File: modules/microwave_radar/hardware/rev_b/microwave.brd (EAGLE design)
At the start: 68.1 x 66 mm, 56 parts, among them J1 MODULE_GENERIC, J2 TC2030-JLINK-L, U1 SAM4LC8AA, U2 TLV62130, U3 MSGEQ7, U4 HB100, U5 OP284E_SEPARATE

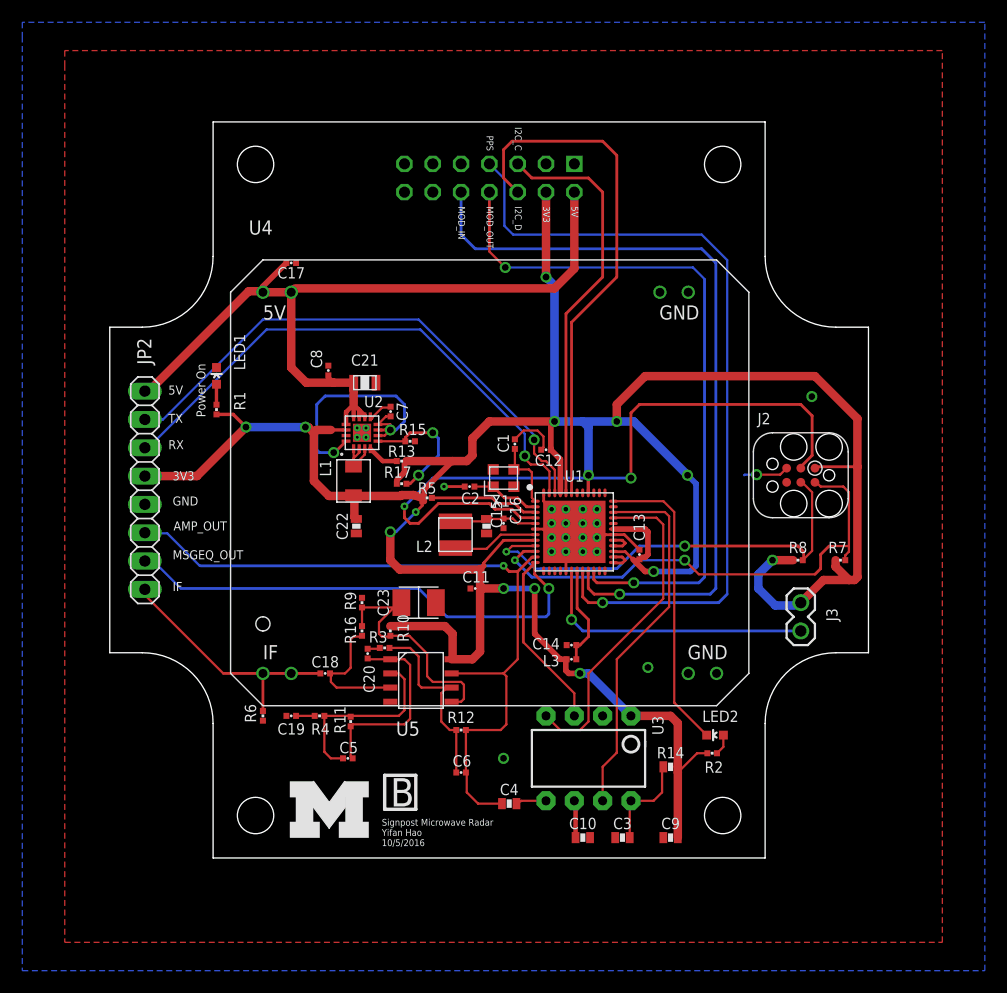
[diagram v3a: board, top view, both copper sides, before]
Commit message: added power gates, almost done routing
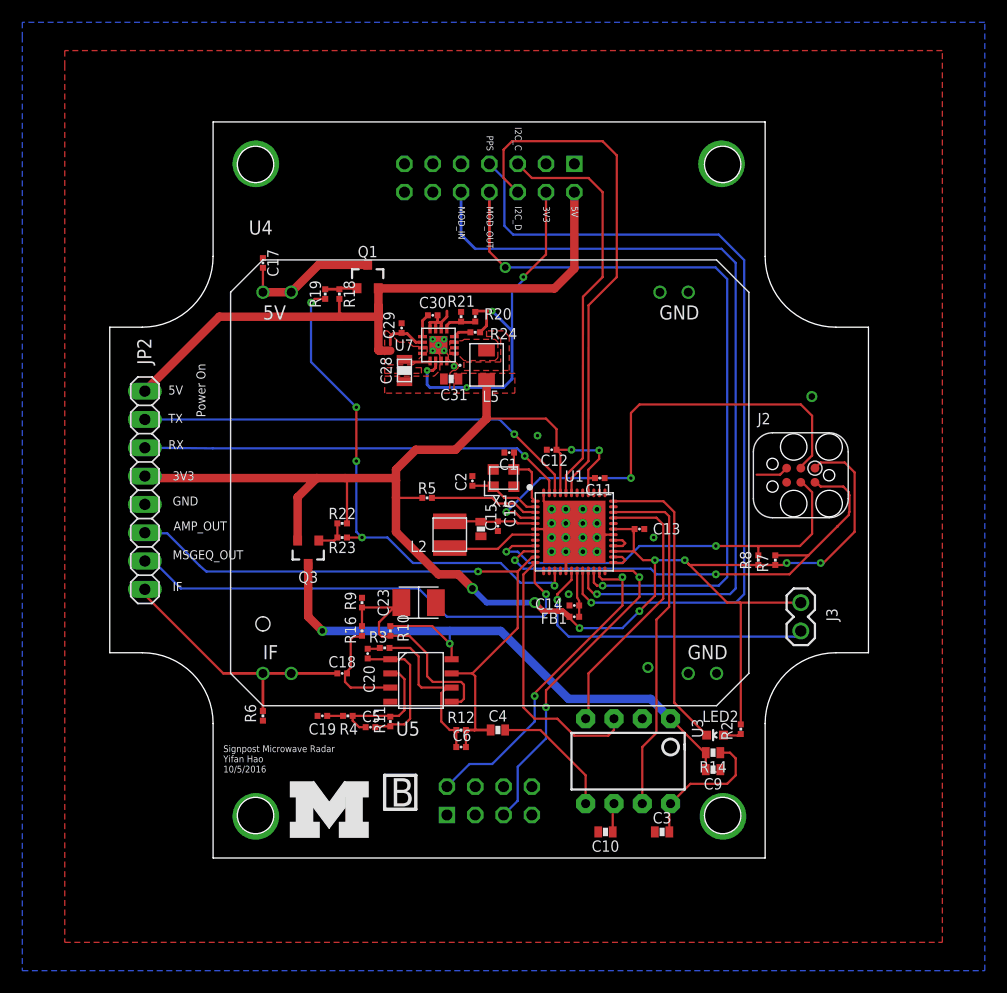
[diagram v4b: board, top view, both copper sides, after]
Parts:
- removed C21: 10uF, passives:0805_CAP
- removed C22: 22uF, passives:0603_CAP
- removed C7: 3.3nF, passives:0402_CAP
- removed C8: 0.1uF, passives:0402_CAP
- removed L1: 2.2uH, passives:IHL-1212BZ-11
- removed L3: 1.5k, passives:0402_CAP
- removed LED1: LED0603, leds:LED-0603
- removed R1: 1k, passives:0402_RES
- removed R13: 100k, passives:0402_RES
- removed R15: 240k, passives:0402_RES
- removed R17: 750k, passives:0402_RES
- removed U2: TLV62130, chips:TQFN-16/3MM
- added C28: 10 uF, passives:0805_CAP
- added C29: 0.1 uF, passives:0402_CAP
- added C30: 3.3 nF, passives:0402_CAP
- added C31: 22 uF, passives:0603_CAP
- added FB1: 1.5k, passives:0402_CAP
- added L5: 2.2 uH, passives:IHL-1212BZ-11
- added Q1, Q3: SI223DDS, fets:SOT23-3
- added R18, R22, R24: 100k, passives:0402_RES
- added R19, R23: 1k, passives:0402_RES
- added R20: 750k, passives:0402_RES
- added R21: 240k, passives:0402_RES
- added U7: TLV62130, chips:TQFN-16/3MM
- J1: value MODULE_GENERIC -> MODULE_GENERIC_DEBUG; device signpost:MODULE_GENERIC -> signpost:MODULE_GENERIC_DEBUG
- R11, R12: value 100k -> 1M
- moved C11 14.9 mm to (46.7, 36.6), turned to 180 degrees
- moved C9 7.19 mm to (56.9, 10.4), turned to 180 degrees
- moved C4 6.68 mm to (37.6, 14.0)
- moved R7 5.84 mm to (62.5, 29.2), turned to 270 degrees
- moved R14 4.02 mm to (56.9, 11.9), turned to 0 degrees
- moved C3 3.59 mm to (52.3, 4.83)
- moved U3 3.57 mm to (49.3, 11.2)
- moved C14 3.57 mm to (44.5, 25.1)
- moved R8 3.56 mm to (61.0, 29.2), turned to 270 degrees
- moved R11 3.56 mm to (27.9, 14.7)
- moved C5 3.45 mm to (26.2, 14.2)
- moved R2 3.35 mm to (59.4, 14.0), turned to 270 degrees
- moved C19 2.79 mm to (21.8, 15.2)
- moved C17 2.54 mm to (16.5, 55.9), turned to 270 degrees
- moved R4 2.54 mm to (24.1, 15.2)
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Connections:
- net CONTROLLER_XIN renamed XIN
- net CONTROLLER_XOUT renamed XOUT
- removed net CONTROLLER_RESET: J2.3, U1.4
- removed net CONTROLLER_SWDCLK: J2.4, R8.1, U1.9
- removed net CONTROLLER_SWDIO: J2.2, R7.1, U1.10
- removed net N$16: U1.15
- removed net N$20: L1.P$1, U2.1, U2.2, U2.3
- removed net N$22: U1.23
- removed net N$23: R13.1, U2.4
- removed net N$24: R15.2, R17.1, U2.5
- removed net N$25: U1.24
- removed net N$4: LED1.A, R1.2
- removed net N$8: C7.1, U2.9
- removed net USART2_RX: JP2.2, U1.46
- removed net USART2_TX: JP2.3, U1.47
- new net !RESET: J1.20, J2.3, U1.4
- new net 3V3_GATED: C9.2, Q3.3, R10.2, R14.1, U3.1, U5.V+
- new net DBG_GPIO1: J1.16, U1.23
- new net DBG_GPIO2: J1.19, U1.24
- new net DBG_RX: J1.18, JP2.2, U1.46
- new net DBG_TX: J1.17, JP2.3, U1.47
- new net N$37: Q1.1, R18.1, R19.2
- new net N$38: Q3.1, R22.1, R23.2
- new net N$42: C30.2, U7.9
- new net N$43: L5.P$1, U7.1, U7.2, U7.3
- new net N$44: R24.1, U7.4
- new net N$45: R20.1, R21.2, U7.5
- new net N$5: C17.2, Q1.3, U4.5V_1, U4.5V_2
- new net RADAR_POWER_GATE: R19.1, R23.1, U1.15
- new net SWDCLK: J1.21, J2.4, R8.1, U1.9
- new net SWDIO: J1.22, J2.2, R7.1, U1.10
- net +3V3: now also C31.2, FB1.2, L5.P$2, Q3.2, R20.2, R22.2, R24.2, U7.14; no longer C22.1, C9.2, L1.P$2, L3.2, R1.1, R10.2, R13.2, R14.1, R17.2, U2.14, U3.1, U5.V+
- net +5V: now also C28.P$1, C29.1, Q1.2, R18.2, U7.10, U7.11, U7.12, U7.13; no longer C17.2, C21.P$1, C8.1, U2.10, U2.11, U2.12, U2.13, U4.5V_1, U4.5V_2
- net GND: now also C28.P$2, C29.2, C30.1, C31.1, J1.15, R21.1, U7.15, U7.16, U7.6, U7.7, U7.8, U7.GND; no longer C21.P$2, C22.2, C7.2, C8.2, LED1.C, R15.1, U2.15, U2.16, U2.6, U2.7, U2.8, U2.GND
- net N$13: now also FB1.1; no longer L3.1
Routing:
- net +3V3: track 278.0 -> 202.7 mm
- net CONTROLLER_RESET: track 63.6 -> 0.00 mm, vias 2 -> 0
- net 3V3_GATED: track 0.00 -> 55.6 mm, vias 0 -> 2
- net USART2_TX: track 49.2 -> 0.00 mm, vias 1 -> 0
- net USART2_RX: track 49.1 -> 0.00 mm, vias 1 -> 0
- net RADAR_POWER_GATE: track 0.00 -> 46.1 mm, vias 0 -> 5
- net CONTROLLER_SWDIO: track 45.5 -> 0.00 mm, vias 2 -> 0
- net SWDIO: track 0.00 -> 43.4 mm, vias 0 -> 2
- net !RESET: track 0.00 -> 43.2 mm, vias 0 -> 2
- net DBG_RX: track 0.00 -> 40.5 mm, vias 0 -> 1
- net CONTROLLER_SWDCLK: track 40.3 -> 0.00 mm, vias 2 -> 0
- net DBG_TX: track 0.00 -> 38.6 mm, vias 0 -> 1
- net SWDCLK: track 0.00 -> 37.7 mm, vias 0 -> 2
- net GND: track 46.8 -> 16.0 mm
- net DBG_GPIO2: track 0.00 -> 29.7 mm, vias 0 -> 2
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- added copper zone on layer 1, net +3V3
- added copper zone on layer 1, net +5V
- added copper zone on layer 1, net N$43
- added copper zone on layer 1, net N$46
- added copper zone on layer 1, net N$47

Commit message: finished routing
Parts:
- removed U$1: (no value), logos:UMICH_SOLID_200MIL
- added U$2: (no value), logos:UMICH_SOLID_75MIL
- added U$3: (no value), logos:UCB_CAL_75MIL
- moved C4 1.52 mm to (36.1, 14.0)
- moved C6 1.27 mm to (33.0, 12.4)
- moved R12 1.27 mm to (33.0, 14.0)
- moved C15 1.14 mm to (35.1, 32.5)
- moved L2 1.14 mm to (32.3, 32.0)
- moved C16 1.05 mm to (36.6, 32.5)
- moved C14 0.25 mm to (44.5, 24.9)
- moved FB1 0.25 mm to (44.5, 23.9)
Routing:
- net DBG_TX: track 38.6 -> 87.9 mm, vias 1 -> 3
- net !RESET: track 43.2 -> 91.6 mm, vias 2 -> 5
- net DBG_RX: track 40.5 -> 86.9 mm, vias 1 -> 5
- net SWDCLK: track 37.7 -> 64.2 mm
- net SWDIO: track 43.4 -> 66.6 mm
- net +3V3: track 202.7 -> 211.8 mm
- net N$3: track 11.4 -> 16.0 mm, vias 0 -> 2
- net AMP_OUT: track 59.0 -> 61.3 mm, vias 1 -> 3
- net N$36: track 8.37 -> 10.0 mm
- net N$6: track 8.21 -> 9.34 mm
- net GND: track 16.0 -> 17.1 mm, vias 27 -> 33
- net DBG_GPIO1: track 29.3 -> 30.2 mm
- net N$19: track 15.0 -> 14.2 mm
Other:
- board text added: "Signpost Microwave Radar Module"
- board text added: "Yifan Hao Joshua Adkins July 2017"
- board text removed: "Signpost Microwave Radar Yifan Hao 10/5/2016"

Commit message: changed values to not have space
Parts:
- C28: value 10 uF -> 10uF
- C29: value 0.1 uF -> 0.1uF
- C30: value 3.3 nF -> 3.3nF
- C31: value 22 uF -> 22uF
- L5: value 2.2 uH -> 2.2uH
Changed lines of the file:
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@@
 <setting verticaltext="up"/>
 </settings>
-<grid distance="5" unitdist="mil" unit="mil" style="lines" multiple="1" display="yes" altdistance="10" altunitdist="mil" altunit="mil"/>
+<grid distance="100" unitdist="mil" unit="mil" style="lines" multiple="1" display="yes" altdistance="10" altunitdist="mil" altunit="mil"/>
 <layers>
 <layer number="1" name="Top" color="4" fill="1" visible="yes" active="yes"/>
@@
 <attribute name="NAME" x="30.036" y="49.018" size="1.016" layer="25" font="vector" ratio="12" rot="R180"/>
 </element>
-<element name="C28" library="passives" package="0805_CAP" value="10 uF" x="29.21" y="46.228" smashed="yes" rot="R90">
+<element name="C28" library="passives" package="0805_CAP" value="10uF" x="29.21" y="46.228" smashed="yes" rot="R90">
 <attribute name="NAME" x="28.067" y="46.228" size="1.016" layer="25" font="vector" ratio="12" rot="R90" align="bottom-center"/>
 </element>
-<element name="C29" library="passives" package="0402_CAP" value="0.1 uF" x="28.956" y="50.038" smashed="yes" rot="R90">
+<element name="C29" library="passives" package="0402_CAP" value="0.1uF" x="28.956" y="50.038" smashed="yes" rot="R90">
 <attribute name="NAME" x="28.321" y="50.292" size="1.016" layer="25" font="vector" ratio="12" rot="R90" align="bottom-center"/>
 </element>
-<element name="C30" library="passives" package="0402_CAP" value="3.3 nF" x="31.75" y="51.181" smashed="yes" rot="R180">
+<element name="C30" library="passives" package="0402_CAP" value="3.3nF" x="31.75" y="51.181" smashed="yes" rot="R180">
 <attribute name="NAME" x="31.75" y="51.816" size="1.016" layer="25" font="vector" ratio="12" align="bottom-center"/>
 </element>
-<element name="C31" library="passives" package="0603_CAP" value="22 uF" x="33.401" y="45.466" smashed="yes">
+<element name="C31" library="passives" package="0603_CAP" value="22uF" x="33.401" y="45.466" smashed="yes">
 <attribute name="NAME" x="33.655" y="44.577" size="1.016" layer="25" font="vector" ratio="12" rot="R180" align="bottom-center"/>
 </element>
@@
 <attribute name="VALUE" x="35.56" y="48.26" size="1.016" layer="27" font="vector" ratio="12" align="bottom-center"/>
 </element>
-<element name="L5" library="passives" package="IHL-1212BZ-11" value="2.2 uH" x="36.576" y="46.736" smashed="yes" rot="R270">
+<element name="L5" library="passives" package="IHL-1212BZ-11" value="2.2uH" x="36.576" y="46.736" smashed="yes" rot="R270">
 <attribute name="DIGIKEY" value="541-1322-1-ND" x="8.636" y="56.896" size="1.778" layer="27" rot="R270" display="off"/>
 <attribute name="NAME" x="37.706" y="44.428" size="1.016" layer="25" font="vector" ratio="12" rot="R180"/>

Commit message: renumbered resistors
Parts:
- removed R21: 240k, passives:0402_RES
- removed R23: 1k, passives:0402_RES
- removed R24: 100k, passives:0402_RES
- added R1: 1k, passives:0402_RES
- added R15: 200k, passives:0603-RES
- added R17: 330k, passives:0402_RES
- R11, R12: value 1M -> 100k
- R14: value 200k -> 100k; device passives:0603-RES -> passives:0402_RES
- R16: value 330k -> 240k
- R18: value 100k -> 750k
- R19: value 1k -> 1M
- R20: value 750k -> 1M
- R3: value 8.2k -> 1k
- R4: value 10k -> 8.2k
- R6: value 12k -> 10k
- R7: value 100k -> 12k
- moved R2 54.0 mm to (22.1, 53.1), turned to 90 degrees
- moved R7 48.0 mm to (16.5, 15.2), turned to 90 degrees
- moved R14 43.3 mm to (35.6, 49.7)
- moved R12 40.3 mm to (23.4, 53.1), turned to 270 degrees
- moved R19 38.8 mm to (27.9, 14.7)
- moved R20 37.2 mm to (33.0, 14.0), turned to 180 degrees
- moved R9 35.8 mm to (61.0, 29.2)
- moved R16 29.6 mm to (34.3, 51.1), turned to 270 degrees
- moved R6 24.5 mm to (31.2, 34.8), turned to 180 degrees
- moved R5 20.8 mm to (24.1, 15.2)
- moved R18 12.4 mm to (35.6, 51.1), turned to 90 degrees
- moved R3 10.6 mm to (23.6, 31.2)
- moved R11 8.13 mm to (27.9, 22.9)
- moved R4 6.93 mm to (27.4, 21.3)
- moved R10 3.59 mm to (25.4, 25.4), turned to 270 degrees
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- renumbered R22 to R13
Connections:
- net +3V3: now also R1.1, R14.2, R18.2, R6.2, R9.2; no longer R2.1, R20.2, R24.2, R5.2, R7.2
- net +5V: now also R12.2; no longer R18.2
- net 3V3_GATED: now also R11.2, R15.1; no longer R10.2, R14.1
- net AMP_OUT: now also R20.1; no longer R12.1
- net GND: now also R10.1, R16.1, R7.1; no longer R21.1, R6.1, R9.1
- net IF: now also R7.2; no longer R6.2
- net N$1: now also R10.2, R11.1, R17.2; no longer R10.1, R16.2, R9.2
- net N$12: now also R19.2, R5.1; no longer R11.2, R4.1
- net N$14: now also R6.1; no longer R5.1
- net N$15: now also R5.2; no longer R4.2
- net N$17: now also R19.1; no longer R11.1
- net N$18: now also R4.2; no longer R3.2
- net N$19: now also R20.2, R4.1; no longer R12.2, R3.1
- net N$2: now also R15.2; no longer R14.2
- net N$34: now also R1.2; no longer R2.2
- net N$37: now also R12.1, R2.2; no longer R18.1, R19.2
- net N$38: now also R3.2; no longer R23.2
- net N$44: now also R14.1; no longer R24.1
- net N$45: now also R16.2, R18.1; no longer R20.1, R21.2
- net N$9: now also R17.1; no longer R16.1
- net RADAR_POWER_GATE: now also R2.1, R3.1; no longer R19.1, R23.1
- net SWDCLK: now also R9.1; no longer R8.1
- net SWDIO: now also R8.1; no longer R7.1

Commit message: silk and renumbering
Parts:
- C15: value 6.8uF -> 100nF; device passives:0603_CAP -> passives:0402_CAP
- C17: value 100nF -> 4.7uF
- C20: value 4.7uF -> 6.8uF; device passives:0402_CAP -> passives:0603_CAP
- J1: value MODULE_GENERIC_DEBUG -> (none); device signpost:MODULE_GENERIC_DEBUG -> umich:1X02
- J2: value TC2030-JLINK-L -> MODULE_GENERIC_DEBUG; device connector:TC2030-IDC -> signpost:MODULE_GENERIC_DEBUG
- J3: value (none) -> TC2030-JLINK-L; device umich:1X02 -> connector:TC2030-IDC
- moved C17 37.5 mm to (23.6, 19.1), turned to 0 degrees
- moved C16 30.8 mm to (16.5, 55.9), turned to 270 degrees
- moved J1 29.7 mm to (64.8, 25.4), turned to 270 degrees
- moved J2 28.0 mm to (36.8, 35.6), turned to 0 degrees
- moved C20 14.8 mm to (35.1, 32.5)
- moved J3 11.4 mm to (64.8, 36.8), turned to 180 degrees
- moved C19 6.91 mm to (25.9, 20.8), turned to 90 degrees
- moved C18 4.20 mm to (21.8, 15.2)
- moved C15 1.52 mm to (36.6, 32.5)
- renumbered C28 to C21, C29 to C8, C30 to C7, C31 to C22, JP2 to JP1, L5 to L1, LED2 to LED1, Q3 to Q2
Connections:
- net !RESET: now also J2.20, J3.3; no longer J1.20, J2.3
- net +3V3: now also J1.1, J2.4; no longer J1.4, J2.1
- net +5V: now also J2.2; no longer J1.2
- net ADVREFP: now also J1.2; no longer J3.2
- net DBG_GPIO1: now also J2.16; no longer J1.16
- net DBG_GPIO2: now also J2.19; no longer J1.19
- net DBG_RX: now also J2.18; no longer J1.18
- net DBG_TX: now also J2.17; no longer J1.17
- net GND: now also C18.1, C20.1, J2.1, J2.14, J2.15, J3.5; no longer C17.1, C19.1, J1.1, J1.14, J1.15, J2.5
- net I2C_CLK: now also J2.5; no longer J1.5
- net I2C_DATA: now also J2.6; no longer J1.6
- net IF: now also C17.1; no longer C18.1
- net MOD_IN: now also J2.10; no longer J1.10
- net MOD_OUT: now also J2.8; no longer J1.8
- net N$15: now also C18.2; no longer C19.2
- net N$17: now also C19.1; no longer C20.1
- net N$18: now also C19.2; no longer C20.2
- net N$28: now also J2.13; no longer J1.13
- net N$36: now also C20.2; no longer C16.2
- net N$5: now also C16.2; no longer C17.2
- net N$9: now also C17.2; no longer C18.2
- net PPS: now also J2.7; no longer J1.7
- net SWDCLK: now also J2.21, J3.4; no longer J1.21, J2.4
- net SWDIO: now also J2.22, J3.2; no longer J1.22, J2.2
- net USB+: now also J2.11; no longer J1.11
- net USB-: now also J2.12; no longer J1.12
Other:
- board text added: "IN"
- board text added: "OUT"
- board text added: "SCL"
- board text added: "SDA"
- board text added: "VCCIO"
- board text removed: "I2C_C"
- board text removed: "I2C_D"
- board text removed: "MOD_IN"
- board text removed: "MOD_OUT"
- board text removed: "Power On"
